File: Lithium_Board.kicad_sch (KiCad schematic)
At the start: 102 parts, among them IC1 BQ25750RRVR, IC2 STM32G030K6T6, IC3 TPS70933DBVR, J1 XT30PW-M, J2 XT30PW-M, J3 XT30PW-F, J4 J_NTC, J5 TSW-105-07-G-S, Q1 MMBT5551LT1G, Q10 SIR870ADP-T1-GE3, Q3 SIR870ADP-T1-GE3, Q4 SIR870ADP-T1-GE3, Q5 SIR870ADP-T1-GE3, Q6 SIR870ADP-T1-GE3, Q7 SIR870ADP-T1-GE3, Q8 SIR870ADP-T1-GE3, Q9 SIR870ADP-T1-GE3

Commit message: Added CELL BALANCING IC
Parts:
- removed C17: 100nF [HV], CAPC1608X95N, symbol C0603C104K1RACAUTO:C0603C104K1RACAUTO
- removed C18: 470nF [HV], CAPC3216X190N, symbol CGA5L2X7R2A474K160AA:CGA5L2X7R2A474K160AA
- removed C19: 2.2uF [HV], CAPC3216X180N, symbol CL31B225KCHSNNE:CL31B225KCHSNNE
- removed C20: 4.7uF [HV], CAPC3225X94N, symbol KAM32LR72A475KU:KAM32LR72A475KU
- removed C22: 4.7uF, CAPC3225X280N, symbol UMJ325AB7475KMHP:UMJ325AB7475KMHP
- removed C23: 10uF, CAPC3225X285N, symbol CL32B106KBVVPLE:CL32B106KBVVPLE
- removed C24: 2.2uF, C1206, symbol C1206C225K5RACTU:C1206C225K5RACTU
- removed C25: 470nF, C0805, symbol C0805X474K5RECAUTO:C0805X474K5RECAUTO
- removed C26: 1uF, CAPC2012X145N, symbol C2012X7R1H105K125AB:C2012X7R1H105K125AB
- removed C27: 220nF, C0805, symbol C0805C224K5RACTU:C0805C224K5RACTU
- removed C28: 150nF, C1210, symbol C1210C154K5RACTU:C1210C154K5RACTU
- removed C29: 56nF, C0603, symbol C0603C563K5RACTU:C0603C563K5RACTU
- removed C30: 1.2nF, C0603, symbol C0603C122K5RACTU:C0603C122K5RACTU
- removed C31: 100nF, CAPC1608X90N, symbol CC0603KRX7R9BB104:CC0603KRX7R9BB104
- removed C32: 10nF, CAPC1608X90N, symbol GCM188R71H103KA37J:GCM188R71H103KA37J
- removed C33: 100uF, EEE1AA101SP, symbol EEE-FT1V101AP:EEE-FT1V101AP
- removed C40: 22nF, C0603, symbol C0603C223K5RACTU:C0603C223K5RACTU
- removed C41: 150pF, CAPC1608X87N, symbol C0603C151J5GACTU:C0603C151J5GACTU
- removed D1: 1N4148WQ-7-F, SOD3716X145N, symbol 1N4148WQ-7-F:1N4148WQ-7-F
- removed J4: J_NTC, symbol Connector_Generic:Conn_01x02
- removed Q1: MMBT5551LT1G, SOT96P237X111-3N, symbol MMBT5551LT1G:MMBT5551LT1G
- removed R20: 2mΩ, RESC3216X59N, symbol PMR18EZPFV2L00:PMR18EZPFV2L00
- removed R21: 5mΩ, RESC6432X67N, symbol PMR100HZPFU5L00:PMR100HZPFU5L00
- removed R22: 1MΩ, RESC3116X65N, symbol VT1206BRD071ML:VT1206BRD071ML
- removed R23: 249k, RESC1608X55N, symbol RC0603FR-07249KL:RC0603FR-07249KL
- removed R24: 34.8k, RESC1608X55N, symbol RC0603FR-0734K8L:RC0603FR-0734K8L
- removed R25: 10k, RESC1608X55N, symbol RC0603FR-0710KL:RC0603FR-0710KL
- removed R26: 4.7k, RESC1608X55N, symbol RC0603FR-074K7L:RC0603FR-074K7L
- removed R28: 30.1k, RESC1608X55N, symbol RC0603FR-0730K1L:RC0603FR-0730K1L
- removed R29: 5.23k, RESC1608X55N, symbol RC0603FR-075K23L:RC0603FR-075K23L
- removed R30: 100k, RESC1608X55N, symbol RC0603FR-07100KL:RC0603FR-07100KL
- removed R31: 100Ω, RESC1608X55N, symbol RC0603FR-07100RL:RC0603FR-07100RL
- removed R32: 10Ω, RESC1608X55N, symbol RC0603FR-0710RL:RC0603FR-0710RL
- removed R33: 2Ω, RESC1608X55N, symbol RC0603FR-072RL:RC0603FR-072RL
- removed R34: 0Ω, ERJ3EKF1000V, symbol ERJ-3GEY0R00V:ERJ-3GEY0R00V
- added C42, C43, C44, C45: 220nF, C0805, symbol C0805C224K5RACTU:C0805C224K5RACTU
- added C46, C50, C53: 1uF, CAPC2012X145N, symbol C2012X7R1H105K125AB:C2012X7R1H105K125AB
- added C47: 150pF, CAPC1608X87N, symbol C0603C151J5GACTU:C0603C151J5GACTU
- added C48: 22nF, C0603, symbol C0603C223K5RACTU:C0603C223K5RACTU
- added C49: 2.2uF, C1206, symbol C1206C225K5RACTU:C1206C225K5RACTU
- added C52: 100pF, CAPC1608X87N, symbol C0603C101J5GACTU:C0603C101J5GACTU
- added D2, D3: 1N4148WQ-7-F, SOD3716X145N, symbol 1N4148WQ-7-F:1N4148WQ-7-F
- added IC4: BQ7694204PFBR, QFP50P900X900X120-48N, symbol BQ7694204PFBR:BQ7694204PFBR
- added J6: Conn_01x06, symbol Connector_Generic:Conn_01x06
- added Q2: MMBT5551LT1G, SOT96P237X111-3N, symbol MMBT5551LT1G:MMBT5551LT1G
- added R20, R21: 4.7k, RESC1608X55N, symbol RC0603FR-074K7L:RC0603FR-074K7L
- added R22, R49, R50: 10k, RESC1608X55N, symbol RC0603FR-0710KL:RC0603FR-0710KL
- added R42, R43, R44, R45, R46, R47: 100Ω, RESC1608X55N, symbol RC0603FR-07100RL:RC0603FR-07100RL
- added R48: 10MΩ, RESC1608X55N, symbol RC0603FR-0710ML:RC0603FR-0710ML
- added R53: 150Ω, RESC1608X55N, symbol RC0603FR-07150RL:RC0603FR-07150RL
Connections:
- net +3V3: now also R20.2, R21.2, R22.2
- net BQ_TS: now also J6.5 (Pin_5)
- net GND: now also C42.2, C46.2, C47.2, C48.2, C49.2, C50.2, C52.2, C53.2, IC4.17 (VSS), IC4.18 (SRP), IC4.20 (SRN), IC4.33 (RST_SHUT), IC4.41 (LD), J6.1 (Pin_1), J6.6 (Pin_6), R43.1, R48.2
- net BQ2_ALERT: now reaches IC2.11 (PA4)
- net BQ2_ALERT: now also IC4.25 (ALERT), R22.1, R49.2
- net BQ2_SCL: now reaches IC2.12 (PA5)
- net BQ2_SCL: now also IC4.26 (SCL), R20.1
- net BQ2_SDA: now reaches IC2.13 (PA6)
- net BQ2_SDA: now also IC4.27 (SDA), R21.1
- net BQ2_HDQ: now reaches IC2.14 (PA7)
- net BQ2_HDQ: now also IC4.28 (HDQ)
- net VBAT renamed +BATT
- net VIN renamed +48V
- new net: C46.1, C52.1, IC4.46 (CP1), IC4.47 (BAT), R47.2
- new net: C44.1, IC4.14 (VC2), R42.2
- new net: D3.1 (K), R53.2
- new net: C48.1, IC4.36 (REGIN), Q2.2 (E)
- new net: C42.1, C43.2, IC4.16 (VC0), R43.2
- new net: C45.1, IC4.48 (VC10), R46.2
- new net: C43.1, C44.2, IC4.15 (VC1), R44.2
- new net: C53.1, Q2.3 (C), R53.1
- new net: C47.1, IC4.37 (BREG), Q2.1 (B), R48.1
- new net: C45.2, IC4.10 (VC5), IC4.12 (VC4), IC4.13 (VC3), IC4.2 (VC9), IC4.4 (VC8), IC4.6 (VC7), IC4.8 (VC6), R45.2
- new net: C50.1, IC4.35 (REG1), R49.1
- new net: D2.1 (K), R47.1
- new net: C49.1, IC4.24 (REG18)
- new net: IC4.42 (PACK), R50.1
- new net BAT1: J6.2 (Pin_2), R44.1
- new net BAT2: J6.3 (Pin_3), R42.1, R45.1
- new net BAT3/PACK+: D2.2 (A), D3.2 (A), J6.4 (Pin_4), R46.1, R50.2
- no-connect marks 7 -> 44
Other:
- note added: "BALANCE BATTERY CONNECTOR"
- note added: "CELL BALANCING"
- moved on the sheet: IC2

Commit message: Added Hierarchical Sheets
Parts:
- removed C42, C43, C44, C45: 220nF, C0805, symbol C0805C224K5RACTU:C0805C224K5RACTU
- removed C46, C50, C53: 1uF, CAPC2012X145N, symbol C2012X7R1H105K125AB:C2012X7R1H105K125AB
- removed C47: 150pF, CAPC1608X87N, symbol C0603C151J5GACTU:C0603C151J5GACTU
- removed C48: 22nF, C0603, symbol C0603C223K5RACTU:C0603C223K5RACTU
- removed C49: 2.2uF, C1206, symbol C1206C225K5RACTU:C1206C225K5RACTU
- removed C52: 100pF, CAPC1608X87N, symbol C0603C101J5GACTU:C0603C101J5GACTU
- removed D2, D3: 1N4148WQ-7-F, SOD3716X145N, symbol 1N4148WQ-7-F:1N4148WQ-7-F
- removed IC2: STM32G030K6T6, QFP80P900X900X160-32N, symbol STM32G030K6T6:STM32G030K6T6
- removed IC4: BQ7694204PFBR, QFP50P900X900X120-48N, symbol BQ7694204PFBR:BQ7694204PFBR
- removed J6: Conn_01x06, symbol Connector_Generic:Conn_01x06
- removed Q2: MMBT5551LT1G, SOT96P237X111-3N, symbol MMBT5551LT1G:MMBT5551LT1G
- removed R20, R21: 4.7k, RESC1608X55N, symbol RC0603FR-074K7L:RC0603FR-074K7L
- removed R22, R49, R50: 10k, RESC1608X55N, symbol RC0603FR-0710KL:RC0603FR-0710KL
- removed R42, R43, R44, R45, R46, R47: 100Ω, RESC1608X55N, symbol RC0603FR-07100RL:RC0603FR-07100RL
- removed R48: 10MΩ, RESC1608X55N, symbol RC0603FR-0710ML:RC0603FR-0710ML
- removed R53: 150Ω, RESC1608X55N, symbol RC0603FR-07150RL:RC0603FR-07150RL
- C1: renamed from C7; footprint CAPC3216X180N -> CL31B225KCHSNNE:CAPC3216X180N
- C10: renamed from C3; footprint CAPC1608X90N -> CC0603KRX7R9BB104:CAPC1608X90N
- C11: renamed from C12; footprint CAPC3225X280N -> UMJ325AB7475KMHP:CAPC3225X280N
- C12: renamed from C11; footprint CAPC3225X280N -> UMJ325AB7475KMHP:CAPC3225X280N
- C13: renamed from C1; footprint CAPC1608X90N -> CC0603KRX7R9BB104:CAPC1608X90N
- C14: renamed from C38; footprint CAPC2012X145N -> C2012X7R1H105K125AB:CAPC2012X145N
- C15: renamed from C37; footprint CAPC1608X90N -> CC0603KRX7R9BB104:CAPC1608X90N
- C16: renamed from C34; footprint CAPC2012X145N -> C2012X7R1H105K125AB:CAPC2012X145N
- C17: renamed from C36; footprint CAPC2012X145N -> C2012X7R1H105K125AB:CAPC2012X145N
- C18: renamed from C14; footprint CAPC3225X94N -> KAM32LR72A475KU:CAPC3225X94N
- C19: renamed from C21; footprint CAPC3225X94N -> KAM32LR72A475KU:CAPC3225X94N
- C2: renamed from C9; footprint CAPC1608X95N -> C0603C104K1RACAUTO:CAPC1608X95N
- C20: renamed from C16; footprint CAPC1608X95N -> C0603C104K1RACAUTO:CAPC1608X95N
- C21: renamed from C39; footprint CAPC1608X90N -> CC0603KRX7R9BB104:CAPC1608X90N
- C22: renamed from C35; footprint CAPC3225X94N -> KAM32LR72A475KU:CAPC3225X94N
- C23: renamed from C15; footprint EEEFK0J682AV -> EEV-FK2A101V:EEEFK0J682AV
- C3: renamed from C10; footprint CAPC1608X95N -> C0603C104K1RACAUTO:CAPC1608X95N
- C4: renamed from C6; footprint C0603 -> C0603C563K5RACTU:C0603
- C5: footprint C0603 -> C0603C563K5RACTU:C0603
- C6: renamed from C8; footprint CAPC3216X190N -> CGA5L2X7R2A474K160AA:CAPC3216X190N
- C7: renamed from C13; footprint CAPC3216X180N -> CL31B225KCHSNNE:CAPC3216X180N
- C8: renamed from C4; value ~ -> 100uF; footprint EEE1AA101SP -> EEE-FT1V101AP:EEE1AA101SP
- C9: renamed from C2; footprint C0805 -> C0805X474K5RECAUTO:C0805
- IC1: footprint QFN50P500X600X100-37N-D -> BQ25750RRVR:QFN50P500X600X100-37N-D
- IC2: renamed from IC3; footprint SOT95P280X145-5N -> TPS70933DBVR:SOT95P280X145-5N
- J1: renamed from J2; footprint XT30PWM -> XT30PW-M:XT30PWM
- J2: renamed from J3; footprint XT30PWF -> XT30PW-F:XT30PWF
- J3: renamed from J1; footprint XT30PWM -> XT30PW-M:XT30PWM
- J5: footprint TSW-105-XX-YY-S -> TSW-105-XX-YY-S:TSW-105-XX-YY-S
- L1: footprint INDPM110100X400N -> SRP1038A-100M:INDPM110100X400N
- Q1: renamed from Q7; footprint POWERPAK-SO-8 -> SIR870ADP-T1-GE3:POWERPAK-SO-8
- Q2: renamed from Q4; footprint POWERPAK-SO-8 -> SIR870ADP-T1-GE3:POWERPAK-SO-8
- Q3: renamed from Q8; footprint POWERPAK-SO-8 -> SIR870ADP-T1-GE3:POWERPAK-SO-8
- Q4: renamed from Q6; footprint POWERPAK-SO-8 -> SIR870ADP-T1-GE3:POWERPAK-SO-8
- Q5: renamed from Q10; footprint POWERPAK-SO-8 -> SIR870ADP-T1-GE3:POWERPAK-SO-8
- Q6: renamed from Q3; footprint POWERPAK-SO-8 -> SIR870ADP-T1-GE3:POWERPAK-SO-8
- Q7: renamed from Q9; footprint POWERPAK-SO-8 -> SIR870ADP-T1-GE3:POWERPAK-SO-8
- Q8: renamed from Q5; footprint POWERPAK-SO-8 -> SIR870ADP-T1-GE3:POWERPAK-SO-8
- R1: renamed from R19; footprint RESC3216X59N -> PMR18EZPFV2L00:RESC3216X59N
- R10: renamed from R27; footprint RESC1608X55N -> RC0603FR-0780K6L:RESC1608X55N
- R11: renamed from R12; footprint RESC1608X55N -> RC0603FR-07249KL:RESC1608X55N
- R12: renamed from R37; footprint RESC1608X55N -> RC0603FR-0710KL:RESC1608X55N
- R13: renamed from R39; footprint RESC1608X55N -> RC0603FR-074K7L:RESC1608X55N
- R14: renamed from R40; footprint RESC1608X55N -> RC0603FR-074K7L:RESC1608X55N
- R15: renamed from R3; footprint RESC1608X55N -> RC0603FR-0710KL:RESC1608X55N
- R16: renamed from R4; footprint RESC1608X55N -> RC0603FR-0710KL:RESC1608X55N
- R17: renamed from R5; footprint RESC1608X55N -> RC0603FR-0710KL:RESC1608X55N
- R18: renamed from R6; footprint RESC1608X55N -> RC0603FR-0710KL:RESC1608X55N
- R19: renamed from R7; footprint RESC1608X55N -> RC0603FR-07100KL:RESC1608X55N
- R2: renamed from R17; footprint RESC1608X55N -> RC0603FR-0710RL:RESC1608X55N
- R20: renamed from R8; footprint RESC1608X55N -> RC0603FR-075K23L:RESC1608X55N
- R21: renamed from R9; footprint RESC1608X55N -> RC0603FR-0730K1L:RESC1608X55N
- R22: renamed from R38; footprint RESC1608X55N -> RC0603FR-0710KL:RESC1608X55N
- R23: renamed from R11; footprint RESC1608X55N -> RC0603FR-0734K8L:RESC1608X55N
- R24: renamed from R10; footprint RESC1608X55N -> RC0603FR-0710KL:RESC1608X55N
- R25: renamed from R13; footprint RESC1608X55N -> RC0603FR-0734K8L:RESC1608X55N
- R26: renamed from R41; footprint RESC1608X55N -> RC0603FR-0710KL:RESC1608X55N
- R27: renamed from R2; footprint RESC1608X55N -> RC0603FR-072RL:RESC1608X55N
- R3: renamed from R18; footprint RESC1608X55N -> RC0603FR-0710RL:RESC1608X55N
- R4: renamed from R1; footprint RESC1608X55N -> RC0603FR-072RL:RESC1608X55N
- R5: renamed from R15; footprint RESC1608X55N -> RC0603FR-0710RL:RESC1608X55N
- R6: renamed from R36; footprint RESC3116X65N -> VT1206BRD071ML:RESC3116X65N
- R7: renamed from R14; footprint RESC6432X67N -> PMR100HZPFU5L00:RESC6432X67N
- R8: renamed from R35; footprint RESC1608X55N -> RC0603FR-07100KL:RESC1608X55N
- R9: renamed from R16; footprint RESC1608X55N -> RC0603FR-0710RL:RESC1608X55N
- Z1: footprint SOT96P237X111-3N -> SZBZX84C15LT3G:SOT96P237X111-3N
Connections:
- no-connect marks 44 -> 7
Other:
- added sheet CELL BALANCING IC (Cell_Balancing.kicad_sch)
- added sheet MCU (mcu.kicad_sch)
- note removed: "BALANCE BATTERY CONNECTOR"
- note removed: "CELL BALANCING"
- note removed: "MCU"
- moved on the sheet: C1, C10, C11, C12, C13, C14, C15, C16, C17, C18, C19, C2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

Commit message: Added Ratings+Net Labels+First Layout Try+Calculations Excel
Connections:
- net SW2: now reaches C5.1, IC1.18 (SW2), L1.2, Q2.1 (S_1), Q2.2 (S_2), Q2.3 (S_3), Q8.5 (D_1), Q8.6 (D_2), Q8.7 (D_3), Q8.8 (D_4)
- net BTST2: now reaches C5.2, IC1.20 (BTST2)
- net SW1: now reaches C4.1, IC1.28 (SW1), L1.1, Q5.1 (S_1), Q5.2 (S_2), Q5.3 (S_3), Q6.5 (D_1), Q6.6 (D_2), Q6.7 (D_3), Q6.8 (D_4)
- net HIDRV1: now reaches IC1.27 (HIDRV1), Q5.4 (G)
- net ILIM_HIZ: now reaches IC1.10 (ILIM_HIZ), R24.2
- net FBG: now reaches IC1.11 (FBG), R25.2
- net SRN: now reaches C13.1, C9.2, IC1.13 (SRN), R9.1
- net SRP: now reaches C10.2, C9.1, IC1.14 (SRP), R5.1
- net HIDRV2: now reaches IC1.19 (HIDRV2), Q2.4 (G)
- net BTST1: now reaches C4.2, IC1.26 (BTST1)
- net ACN: now reaches C3.2, C6.2, IC1.29 (ACN), R3.2
- net ACP: now reaches C2.1, C6.1, IC1.30 (ACP), R2.2
- net ACDRV: now reaches IC1.31 (ACDRV), Q1.4 (G), Q4.4 (G), Z1.3 (K)
- net VAC: now reaches C7.1, IC1.33 (VAC), R4.1
- net FSW_SYNC: now reaches IC1.36 (FSW__SYNC), R10.1
- net ICHG: now reaches IC1.9 (ICHG), R23.2
- net Q7_DRAIN: now reaches C8.1 (+), Q2.5 (D_1), Q2.6 (D_2), Q2.7 (D_3), Q2.8 (D_4), Q7.5 (D_1), Q7.6 (D_2), Q7.7 (D_3), Q7.8 (D_4), R5.2, R7.1
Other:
- note added: "0.1W"
- note added: "0.25W"
- note added: "100V"
- note added: "1W"
- note added: "2W"
- note added: "35V"
- note added: "50V"
- note added: "7.5A"

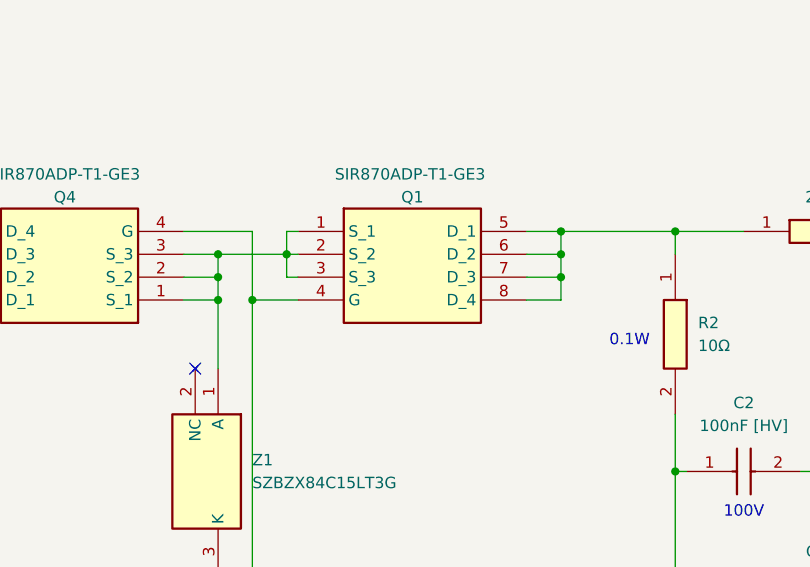
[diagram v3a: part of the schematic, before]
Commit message: New Cleaner Layout + Cell Balancing Connector
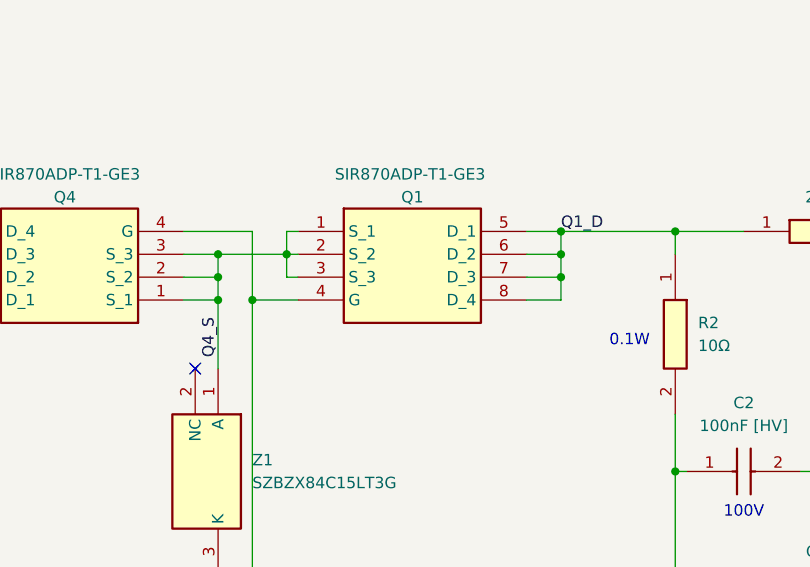
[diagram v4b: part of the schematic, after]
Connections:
- net Q4_S: now reaches Q1.1 (S_1), Q1.2 (S_2), Q1.3 (S_3), Q4.1 (S_1), Q4.2 (S_2), Q4.3 (S_3), Z1.1 (A)
- net Q1_D: now reaches Q1.5 (D_1), Q1.6 (D_2), Q1.7 (D_3), Q1.8 (D_4), R1.1, R2.1
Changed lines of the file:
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@@
+		)
+	)
+	(label "Q4_S"
+		(at 137.16 81.28 90)
+		(effects
+			(font
+				(size 1.27 1.27)
+			)
+			(justify left bottom)
 		)
 	)
@@
 		)
 	)
+	(label "Q1_D"
+		(at 175.26 67.31 0)
+		(effects
+			(font
+				(size 1.27 1.27)
+			)
+			(justify left bottom)
+		)
+	)
